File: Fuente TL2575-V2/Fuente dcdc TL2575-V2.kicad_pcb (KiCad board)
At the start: 2 copper layers, 55.9 x 38.1 mm, 22 parts, among them U1 TL2575

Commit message: Modificando la version 2 de la fuente TL2575
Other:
- board text added: "DC/DC-1A-V2-2015-PFM"
- board text removed: "DC/DC-1A-V2 PFM"
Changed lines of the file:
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@@
   (general
     (links 35)
-    (no_connects 1)
+    (no_connects 0)
     (area 85.28143 32.075 158.950046 77.69626)
     (thickness 1.6)
@@
       (effects (font (size 1 1) (thickness 0.15)))
     )
-    (fp_text value 1pin (at 0 2.794) (layer F.Fab)
+    (fp_text value 1pin (at 0 2.794) (layer F.Fab) hide
       (effects (font (size 1 1) (thickness 0.15)))
     )
@@
       (effects (font (size 1 1) (thickness 0.15)))
     )
-    (fp_text value 1pin (at 0 2.794) (layer F.Fab)
+    (fp_text value 1pin (at 0 2.794) (layer F.Fab) hide
       (effects (font (size 1 1) (thickness 0.15)))
     )
@@
       (effects (font (size 1 1) (thickness 0.15)))
     )
-    (fp_text value 1pin (at 0 2.794) (layer F.Fab)
+    (fp_text value 1pin (at 0 2.794) (layer F.Fab) hide
       (effects (font (size 1 1) (thickness 0.15)))
     )
@@
       (effects (font (size 1 1) (thickness 0.15)))
     )
-    (fp_text value 1pin (at 0 2.794) (layer F.Fab)
+    (fp_text value 1pin (at 0 2.794) (layer F.Fab) hide
       (effects (font (size 1 1) (thickness 0.15)))
     )
@@
     )
   )
-  (gr_text "DC/DC-1A-V2\nPFM\n" (at 129.54 40.64) (layer F.SilkS)
+  (gr_text "DC/DC-1A-V2-2015-PFM\n" (at 120.015 39.37) (layer F.SilkS)
     (effects (font (size 1.5 1.5) (thickness 0.3)))
   )

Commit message: Finalizando TL2575-V2
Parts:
- added C6: 100nF, Capacitors_ThroughHole:C_Disc_D3_P2.5, F.Cu at (128.3, 48.8)
- R2: moved to F.Cu
- Vin1: value CONN_01X03 -> VIN
- Vout1: value CONN_01X02 -> VOUT
- moved C4 5.18 mm to (144.0, 55.2), turned to 0 degrees
- moved R2 3.81 mm to (119.4, 38.1)
- moved REF** 3.59 mm to (147.3, 38.1)
- moved Vout1 3.18 mm to (144.8, 62.2)
- moved REF** 2.54 mm to (147.3, 71.1)
- moved REF** 2.54 mm to (101.6, 38.1)
- moved Vin1 1.27 mm to (104.1, 54.6)
- moved C3 0.21 mm to (137.2, 60.2)
- moved C5 0.17 mm to (137.2, 67.9)
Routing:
- net Net-(R2-Pad1): track 1.27 -> 5.08 mm
- net Net-(D2-Pad1): track 3.81 -> 5.08 mm
- net Net-(D3-Pad1): track 5.08 -> 5.61 mm
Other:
- board size 55.9 x 38.1 mm -> 53.3 x 40.6 mm
- board text added: "AC/DC-V2 PFM-2015"
- board text added: "OUT:1.23-30VDC/1A"
- board text removed: "DC/DC-1A-V2-2015-PFM"
- board text removed: "OUT:1.23-30VDC"

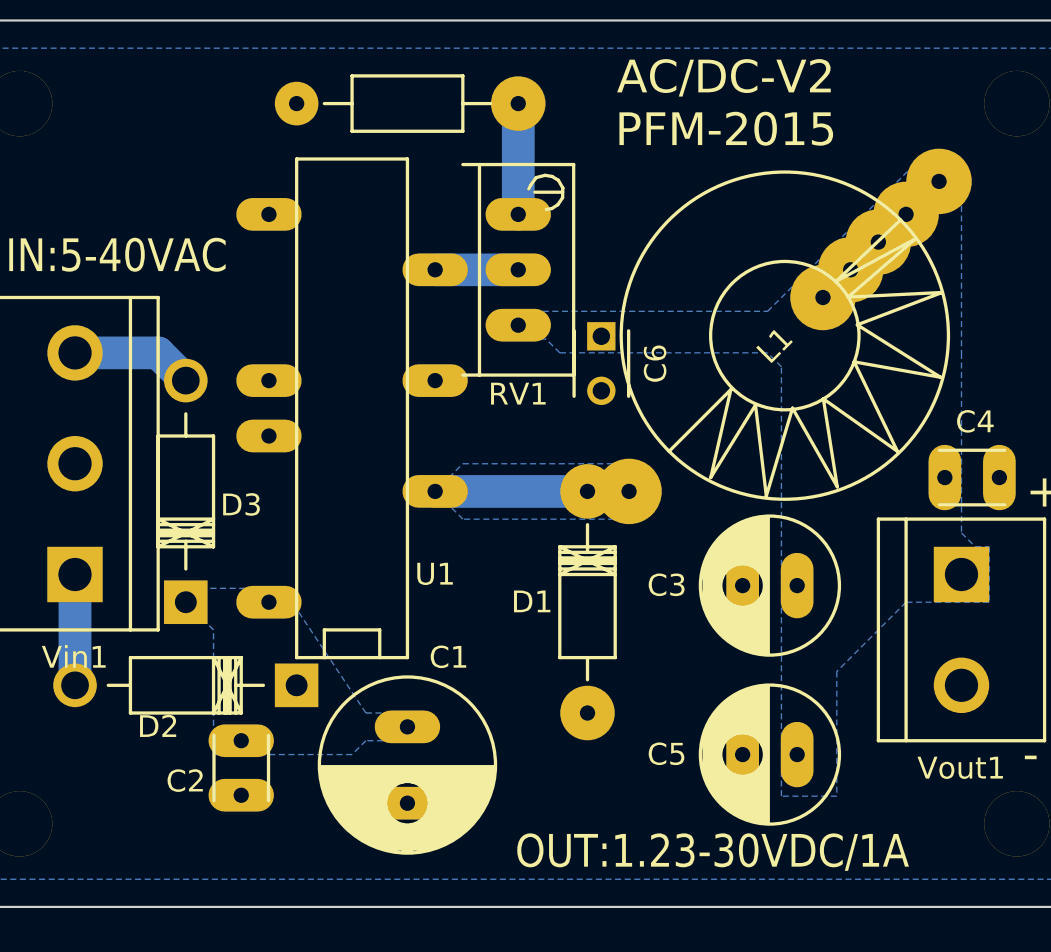
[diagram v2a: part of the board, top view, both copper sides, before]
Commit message: Modificacxiones meores a la fuente TL2575 V2
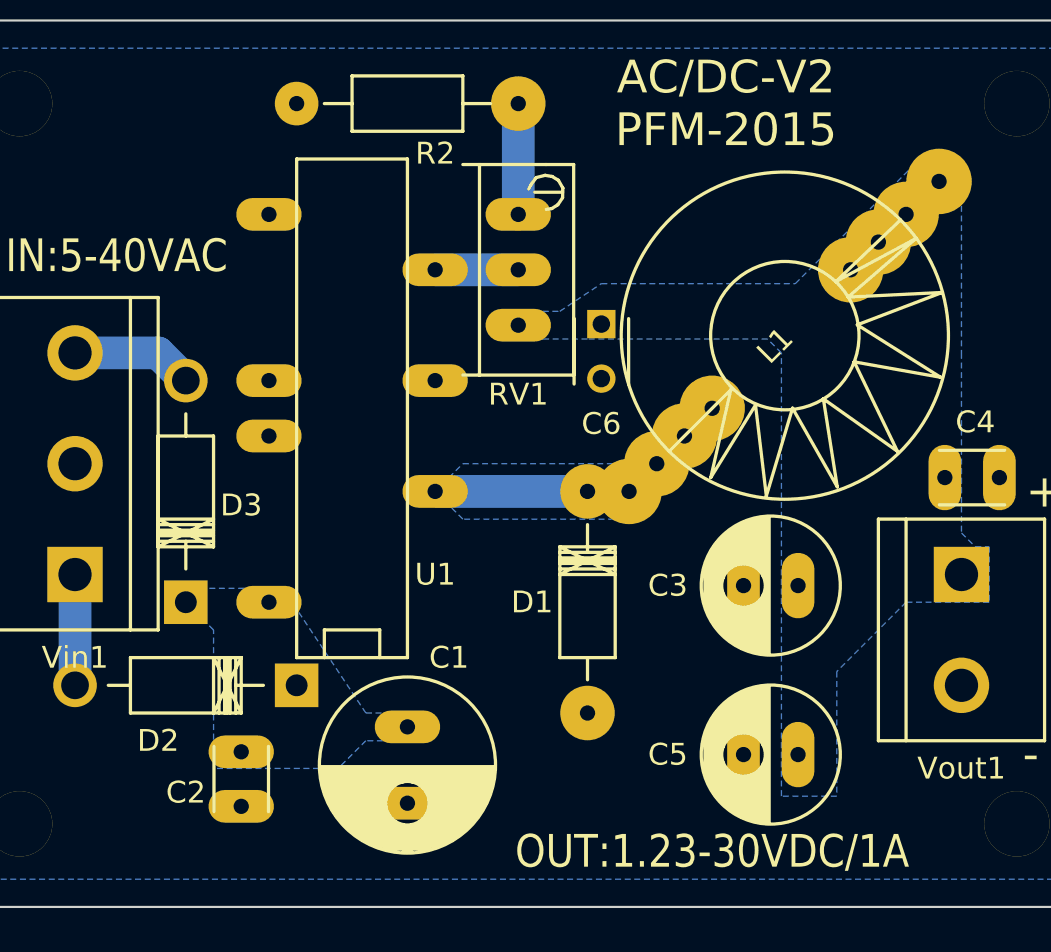
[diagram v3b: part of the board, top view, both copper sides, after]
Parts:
- removed the REF** at (138.4, 47.0)
- added REF**: 1pin, Connect:1pin, F.Cu at (133.3, 52.1)
- added REF**: 1pin, Connect:1pin, F.Cu at (132.1, 53.3)
- added REF**: 1pin, Connect:1pin, F.Cu at (130.8, 54.6)
- moved C6 0.56 mm to (128.3, 48.2)
- moved C2 0.51 mm to (111.8, 67.8)
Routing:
- net Net-(D1-Pad2): track 8.89 -> 14.3 mm
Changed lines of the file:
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@@
 (kicad_pcb (version 4) (host pcbnew "(after 2015-mar-04 BZR unknown)-product")
   (general
-    (links 37)
+    (links 39)
     (no_connects 0)
-    (area 97.739999 34.239999 151.180001 74.980001)
+    (area 85.28143 28.9 156.410046 77.69626)
     (thickness 1.6)
     (drawings 12)
-    (tracks 7)
+    (tracks 10)
     (zones 0)
-    (modules 23)
+    (modules 25)
     (nets 9)
   )
@@
     (mod_text_size 1 1)
     (mod_text_width 0.15)
-    (pad_size 3 1.5)
+    (pad_size 2.99974 2.99974)
     (pad_drill 0.7)
     (pad_to_mask_clearance 0)
@@
       (hpglpendiameter 15)
       (hpglpenoverlay 2)
-      (psnegative false)
+      (psnegative true)
       (psa4output false)
       (plotreference true)
-      (plotvalue true)
+      (plotvalue false)
       (plotinvisibletext false)
       (padsonsilk false)
       (subtractmaskfromsilk false)
-      (outputformat 1)
+      (outputformat 4)
       (mirror false)
-      (drillshape 0)
+      (drillshape 1)
       (scaleselection 1)
       (outputdirectory ""))
@@
   )
   (module Connect:1pin (layer F.Cu)
+    (at 133.35 52.07)
+    (descr "module 1 pin (ou trou mecanique de percage)")
+    (tags DEV)
+    (fp_text reference REF** (at 0 -3.048) (layer F.SilkS) hide
+      (effects (font (size 1 1) (thickness 0.15)))
+    )
+    (fp_text value 1pin (at 0 2.794) (layer F.Fab) hide
+      (effects (font (size 1 1) (thickness 0.15)))
+    )
+    (pad 1 thru_hole circle (at 0 0) (size 2.99974 2.99974) (drill 0.7) (layers *.Cu *.Mask F.SilkS)
+      (net 4 "Net-(D1-Pad2)"))
+  )
+  (module Connect:1pin (layer F.Cu)
+    (at 132.08 53.34)
+    (descr "module 1 pin (ou trou mecanique de percage)")
+    (tags DEV)
+    (fp_text reference REF** (at 0 -3.048) (layer F.SilkS) hide
+      (effects (font (size 1 1) (thickness 0.15)))
+    )
+    (fp_text value 1pin (at 0 2.794) (layer F.Fab) hide
+      (effects (font (size 1 1) (thickness 0.15)))
+    )
+    (pad 1 thru_hole circle (at 0 0) (size 2.99974 2.99974) (drill 0.7) (layers *.Cu *.Mask F.SilkS)
+      (net 4 "Net-(D1-Pad2)"))
+  )
+  (module Connect:1pin (layer F.Cu)
+    (at 130.81 54.61)
+    (descr "module 1 pin (ou trou mecanique de percage)")
+    (tags DEV)
+    (fp_text reference REF** (at 0 -3.048) (layer F.SilkS) hide
+      (effects (font (size 1 1) (thickness 0.15)))
+    )
+    (fp_text value 1pin (at 0 2.794) (layer F.Fab) hide
+      (effects (font (size 1 1) (thickness 0.15)))
+    )
+    (pad 1 thru_hole circle (at 0 0) (size 2.99974 2.99974) (drill 0.7) (layers *.Cu *.Mask F.SilkS)
+      (net 4 "Net-(D1-Pad2)"))
+  )
+  (module Connect:1pin (layer F.Cu)
     (at 140.97 44.45)
     (descr "module 1 pin (ou trou mecanique de percage)")
@@
   (module Connect:1pin (layer F.Cu)
     (at 139.7 45.72)
-    (descr "module 1 pin (ou trou mecanique de percage)")
-    (tags DEV)
-    (fp_text reference REF** (at 0 -3.048) (layer F.SilkS) hide
-      (effects (font (size 1 1) (thickness 0.15)))
-    )
-    (fp_text value 1pin (at 0 2.794) (layer F.Fab) hide
-      (effects (font (size 1 1) (thickness 0.15)))
-    )
-    (pad 1 thru_hole circle (at 0 0) (size 2.99974 2.99974) (drill 0.7) (layers *.Cu *.Mask F.SilkS)
-      (net 3 "Net-(C3-Pad1)"))
-  )
-  (module Connect:1pin (layer F.Cu)
-    (at 138.43 46.99)
     (descr "module 1 pin (ou trou mecanique de percage)")
     (tags DEV)
@@
     (descr "Resistor, Axial,  RM 10mm, 1/3W,")
     (tags "Resistor, Axial, RM 10mm, 1/3W,")
-    (fp_text reference R2 (at -1.27 1.27 180) (layer B.SilkS)
-      (effects (font (size 1 1) (thickness 0.15)) (justify mirror))
+    (fp_text reference R2 (at -1.27 -2.286 180) (layer F.SilkS)
+      (effects (font (size 1 1) (thickness 0.15)))
     )
     (fp_text value R (at 3.81 3.81 180) (layer F.Fab) hide
@@
   )
   (module Capacitors_ThroughHole:C_Radial_D6.3_L11.2_P2.5 (layer F.Cu)
-    (at 137.247 60.198 180)
+    (at 137.287 60.198 180)
     (descr "Radial Electrolytic Capacitor, Diameter 6.3mm x Length 11.2mm, Pitch 2.5mm")
     (tags "Electrolytic Capacitor")
@@
   )
   (module Capacitors_ThroughHole:C_Disc_D3_P2.5 (layer F.Cu)
-    (at 111.76 67.31 270)
+    (at 111.76 67.818 270)
     (descr "Capacitor 3mm Disc, Pitch 2.5mm")
     (tags Capacitor)
@@
     (descr "Diode, DO-41, SOD81, Horizontal, RM 10mm,")
     (tags "Diode, DO-41, SOD81, Horizontal, RM 10mm, 1N4007, SB140,")
-    (fp_text reference D2 (at -1.27 1.905) (layer F.SilkS)
+    (fp_text reference D2 (at -1.27 2.54) (layer F.SilkS)
       (effects (font (size 1 1) (thickness 0.15)))
     )
@@
   )
   (module Capacitors_ThroughHole:C_Radial_D6.3_L11.2_P2.5 (layer F.Cu)
-    (at 137.247 67.945 180)
+    (at 137.287 67.945 180)
     (descr "Radial Electrolytic Capacitor, Diameter 6.3mm x Length 11.2mm, Pitch 2.5mm")
     (tags "Electrolytic Capacitor")
@@
   )
   (module Capacitors_ThroughHole:C_Disc_D3_P2.5 (layer F.Cu)
-    (at 128.27 48.768 270)
+    (at 128.27 48.2092 270)
     (descr "Capacitor 3mm Disc, Pitch 2.5mm")
     (tags Capacitor)
-    (fp_text reference C6 (at 1.25 -2.5 270) (layer F.SilkS)
+    (fp_text reference C6 (at 4.572 0 360) (layer F.SilkS)
       (effects (font (size 1 1) (thickness 0.15)))
     )
@@
   (segment (start 120.65 55.88) (end 127.635 55.88) (width 1.5) (layer B.Cu) (net 4) (status 30))
   (segment (start 127.635 55.88) (end 129.54 55.88) (width 1.5) (layer B.Cu) (net 4) (status 30))
+  (segment (start 129.54 55.88) (end 130.81 54.61) (width 1.5) (layer B.Cu) (net 4))
+  (segment (start 130.81 54.61) (end 132.08 53.34) (width 1.5) (layer B.Cu) (net 4))
+  (segment (start 132.08 53.34) (end 133.35 52.07) (width 1.5) (layer B.Cu) (net 4))
   (segment (start 124.46 43.18) (end 124.46 38.1) (width 1.5) (layer B.Cu) (net 5) (status 30))
   (segment (start 120.65 45.72) (end 124.46 45.72) (width 1.5) (layer B.Cu) (net 6) (status 30))
@@
       (pts
         (xy 146.05 60.96) (xy 142.24 60.96) (xy 139.065 64.135) (xy 139.065 69.85) (xy 136.525 69.85)
-        (xy 136.525 50.165) (xy 135.89 49.53) (xy 126.365 49.53) (xy 125.73 48.895) (xy 123.825 48.895)
-        (xy 123.825 47.625) (xy 135.89 47.625) (xy 142.875 40.64) (xy 144.145 40.64) (xy 144.78 41.91)
-        (xy 144.78 49.53) (xy 144.78 57.785) (xy 145.415 58.42) (xy 146.05 58.42)
+        (xy 136.525 49.53) (xy 135.89 48.895) (xy 127.635 48.895) (xy 125.73 48.895) (xy 123.825 48.895)
+        (xy 123.825 47.625) (xy 126.365 47.625) (xy 128.27 46.355) (xy 137.16 46.355) (xy 142.875 40.64)
+        (xy 144.145 40.64) (xy 144.78 41.91) (xy 144.78 49.53) (xy 144.78 57.785) (xy 145.415 58.42)
+        (xy 146.05 58.42)
       )
     )
@@
     (polygon
       (pts
-        (xy 108.585 60.325) (xy 113.665 60.325) (xy 117.475 66.04) (xy 120.015 66.04) (xy 120.015 67.31)
-        (xy 117.475 67.31) (xy 116.84 67.945) (xy 110.49 67.945) (xy 110.49 62.23) (xy 109.855 61.595)
-        (xy 108.585 61.595)
+        (xy 108.585 60.325) (xy 109.855 60.325) (xy 111.76 60.325) (xy 113.665 60.325) (xy 117.475 66.04)
+        (xy 120.015 66.04) (xy 120.015 67.31) (xy 117.475 67.31) (xy 116.205 68.58) (xy 110.49 68.58)
+        (xy 110.49 62.23) (xy 109.855 61.595) (xy 108.585 61.595)
       )
     )

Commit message: No mucho
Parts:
- moved C1 79.9 mm to (40.6, 53.3), turned to 0 degrees
- moved C6 79.0 mm to (50.8, 33.0)
- moved REF** 79.0 mm to (54.6, 38.1)
- moved REF** 79.0 mm to (64.8, 27.9)
- moved C2 79.0 mm to (34.3, 52.6)
- moved C3 79.0 mm to (59.8, 45.0)
- moved C4 79.0 mm to (66.5, 40.0)
- moved C5 79.0 mm to (59.8, 52.7)
- moved D1 79.0 mm to (50.2, 45.7)
- moved D2 79.0 mm to (31.8, 49.5)
- moved D3 79.0 mm to (31.8, 40.6)
- moved R2 79.0 mm to (41.9, 22.9)
- moved REF** 79.0 mm to (55.9, 36.8)
- moved REF** 79.0 mm to (69.8, 55.9)
- moved REF** 79.0 mm to (53.3, 39.4)
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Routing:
- net Net-(D1-Pad2): track 14.3 -> 7.29 mm
